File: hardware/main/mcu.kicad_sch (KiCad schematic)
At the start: 0 parts

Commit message: hardware: footprints for every part, LCSC library, real A1S pin plan
- lib/lcsc: ESP32-A1S, NS4150B, FS8205A, MSK12C02, PJ-320D imported
  from LCSC with easyeda2kicad (3D paths fixed, NPTH pegs, A1S antenna
  keepout and courtyard), registered in all three projects.
- Parts table with footprint and LCSC number in hardware/README.md.
- The A1S keeps the codec's I2C/I2S inside: display moves to the
  ST7789's pins 14/13/15/22 (SPI or I2C), LED to 12, CHRG/STDBY to 4/2
  through BAT54W. J_SW and J_CHG for an off-board switch and charge LEDs.
- Block sheets use the module's real outputs (HPOUTL/R, SPOLP/N, SPORP/N).

Co-Authored-By: Claude Opus 5.5 <noreply@anthropic.com>
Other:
- note added: "MCU block. To draw here: ESP32-A1S (ES8388; codec I2C/I2S are inside the module), 22u + 100n, EN 10k + 1u, Boot and Reset buttons, 10k pull-ups on GPIO36/39, 10k pull-down on GPIO12 (LED), display: SCK 14, MOSI/SDA 13, CS 15, DC 22; 4.7k pull-ups on 13/14 fitted for I2C only. CHRG 4, STDBY 2. Unused: MIC/LINEIN pins."
- note removed: "MCU block. To draw here: ESP32-A1S (ES8388), 22u + 100n, EN 10k + 1u, Boot and Reset buttons, status LED (GPIO22), I2C pull-ups 4.7k, 10k pull-ups on GPIO36/39. Unused: GPIO12, 16, 17, 35."
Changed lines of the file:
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@@
 		(rev "A")
 	)
-	(text "MCU block. To draw here:\nESP32-A1S (ES8388), 22u + 100n, EN 10k + 1u, Boot and Reset buttons,\nstatus LED (GPIO22), I2C pull-ups 4.7k, 10k pull-ups on GPIO36/39.\nUnused: GPIO12, 16, 17, 35."
+	(text "MCU block. To draw here:\nESP32-A1S (ES8388; codec I2C/I2S are inside the module), 22u + 100n, EN 10k + 1u,\nBoot and Reset buttons, 10k pull-ups on GPIO36/39, 10k pull-down on GPIO12 (LED),\ndisplay: SCK 14, MOSI/SDA 13, CS 15, DC 22; 4.7k pull-ups on 13/14 fitted for I2C only.\nCHRG 4, STDBY 2. Unused: MIC/LINEIN pins."
 		(exclude_from_sim no)
 		(at 101.6 40.64 0)
@@
 		)
 	)
-	(hierarchical_label "BTN6"
+	(hierarchical_label "U0TXD"
+		(shape output)
+		(at 50.8 55.88 180)
+		(effects
+			(font
+				(size 1.27 1.27)
+			)
+			(justify right)
+		)
+	)
+	(hierarchical_label "LED"
+		(shape output)
+		(at 50.8 172.72 180)
+		(effects
+			(font
+				(size 1.27 1.27)
+			)
+			(justify right)
+		)
+	)
+	(hierarchical_label "BTN1"
 		(shape input)
 		(at 50.8 147.32 180)
@@
 		)
 	)
-	(hierarchical_label "U0TXD"
-		(shape output)
-		(at 50.8 55.88 180)
-		(effects
-			(font
-				(size 1.27 1.27)
-			)
-			(justify right)
-		)
-	)
-	(hierarchical_label "BTN1"
-		(shape input)
-		(at 50.8 127 180)
-		(effects
-			(font
-				(size 1.27 1.27)
-			)
-			(justify right)
-		)
-	)
-	(hierarchical_label "STDBY"
-		(shape input)
-		(at 50.8 76.2 180)
+	(hierarchical_label "CHRG"
+		(shape input)
+		(at 50.8 71.12 180)
 		(effects
 			(font
@@
 	(hierarchical_label "BTN3"
 		(shape input)
-		(at 50.8 132.08 180)
-		(effects
-			(font
-				(size 1.27 1.27)
-			)
-			(justify right)
-		)
-	)
-	(hierarchical_label "SDA"
-		(shape bidirectional)
-		(at 50.8 116.84 180)
-		(effects
-			(font
-				(size 1.27 1.27)
-			)
-			(justify right)
-		)
-	)
-	(hierarchical_label "VBAT_SENSE"
-		(shape input)
-		(at 50.8 81.28 180)
+		(at 50.8 152.4 180)
+		(effects
+			(font
+				(size 1.27 1.27)
+			)
+			(justify right)
+		)
+	)
+	(hierarchical_label "SPORP"
+		(shape output)
+		(at 50.8 106.68 180)
+		(effects
+			(font
+				(size 1.27 1.27)
+			)
+			(justify right)
+		)
+	)
+	(hierarchical_label "DISP_CS"
+		(shape output)
+		(at 50.8 137.16 180)
+		(effects
+			(font
+				(size 1.27 1.27)
+			)
+			(justify right)
+		)
+	)
+	(hierarchical_label "BTN5"
+		(shape input)
+		(at 50.8 162.56 180)
+		(effects
+			(font
+				(size 1.27 1.27)
+			)
+			(justify right)
+		)
+	)
+	(hierarchical_label "HP_DET"
+		(shape input)
+		(at 50.8 121.92 180)
 		(effects
 			(font
@@
 		)
 	)
+	(hierarchical_label "EN"
+		(shape input)
+		(at 50.8 60.96 180)
+		(effects
+			(font
+				(size 1.27 1.27)
+			)
+			(justify right)
+		)
+	)
+	(hierarchical_label "DISP_SCK"
+		(shape output)
+		(at 50.8 127 180)
+		(effects
+			(font
+				(size 1.27 1.27)
+			)
+			(justify right)
+		)
+	)
 	(hierarchical_label "AMP_EN"
 		(shape output)
-		(at 50.8 106.68 180)
+		(at 50.8 116.84 180)
+		(effects
+			(font
+				(size 1.27 1.27)
+			)
+			(justify right)
+		)
+	)
+	(hierarchical_label "SPOLP"
+		(shape output)
+		(at 50.8 96.52 180)
+		(effects
+			(font
+				(size 1.27 1.27)
+			)
+			(justify right)
+		)
+	)
+	(hierarchical_label "VBAT_SENSE"
+		(shape input)
+		(at 50.8 81.28 180)
 		(effects
 			(font
@@
 		)
 	)
-	(hierarchical_label "EN"
-		(shape input)
-		(at 50.8 60.96 180)
-		(effects
-			(font
-				(size 1.27 1.27)
-			)
-			(justify right)
-		)
-	)
-	(hierarchical_label "ROUT1"
+	(hierarchical_label "DISP_MOSI"
+		(shape bidirectional)
+		(at 50.8 132.08 180)
+		(effects
+			(font
+				(size 1.27 1.27)
+			)
+			(justify right)
+		)
+	)
+	(hierarchical_label "HPOUTL"
+		(shape output)
+		(at 50.8 86.36 180)
+		(effects
+			(font
+				(size 1.27 1.27)
+			)
+			(justify right)
+		)
+	)
+	(hierarchical_label "SPOLN"
+		(shape output)
+		(at 50.8 101.6 180)
+		(effects
+			(font
+				(size 1.27 1.27)
+			)
+			(justify right)
+		)
+	)
+	(hierarchical_label "STDBY"
+		(shape input)
+		(at 50.8 76.2 180)
+		(effects
+			(font
+				(size 1.27 1.27)
+			)
+			(justify right)
+		)
+	)
+	(hierarchical_label "BTN4"
+		(shape input)
+		(at 50.8 157.48 180)
+		(effects
+			(font
+				(size 1.27 1.27)
+			)
+			(justify right)
+		)
+	)
+	(hierarchical_label "DISP_DC"
+		(shape output)
+		(at 50.8 142.24 180)
+		(effects
+			(font
+				(size 1.27 1.27)
+			)
+			(justify right)
+		)
+	)
+	(hierarchical_label "HPOUTR"
 		(shape output)
 		(at 50.8 91.44 180)
@@
 		)
 	)
-	(hierarchical_label "LOUT1"
-		(shape output)
-		(at 50.8 86.36 180)
-		(effects
-			(font
-				(size 1.27 1.27)
-			)
-			(justify right)
-		)
-	)
-	(hierarchical_label "BTN5"
-		(shape input)
-		(at 50.8 142.24 180)
-		(effects
-			(font
-				(size 1.27 1.27)
-			)
-			(justify right)
-		)
-	)
-	(hierarchical_label "ROUT2"
-		(shape output)
-		(at 50.8 101.6 180)
-		(effects
-			(font
-				(size 1.27 1.27)
-			)
-			(justify right)
-		)
-	)
-	(hierarchical_label "LOUT2"
-		(shape output)
-		(at 50.8 96.52 180)
-		(effects
-			(font
-				(size 1.27 1.27)
-			)
-			(justify right)
-		)
-	)
-	(hierarchical_label "HP_DET"
-		(shape input)
+	(hierarchical_label "SPORN"
+		(shape output)
 		(at 50.8 111.76 180)
 		(effects
@@
 		)
 	)
-	(hierarchical_label "CHRG"
-		(shape input)
-		(at 50.8 71.12 180)
-		(effects
-			(font
-				(size 1.27 1.27)
-			)
-			(justify right)
-		)
-	)
-	(hierarchical_label "LED"
-		(shape output)
-		(at 50.8 152.4 180)
-		(effects
-			(font
-				(size 1.27 1.27)
-			)
-			(justify right)
-		)
-	)
-	(hierarchical_label "SCL"
-		(shape output)
-		(at 50.8 121.92 180)
-		(effects
-			(font
-				(size 1.27 1.27)
-			)
-			(justify right)
-		)
-	)
-	(hierarchical_label "BTN4"
-		(shape input)
-		(at 50.8 137.16 180)
-		(effects
-			(font
+	(hierarchical_label "BTN6"
+		(shape input)
+		(at 50.8 167.64 180)
+		(effects
+			(font

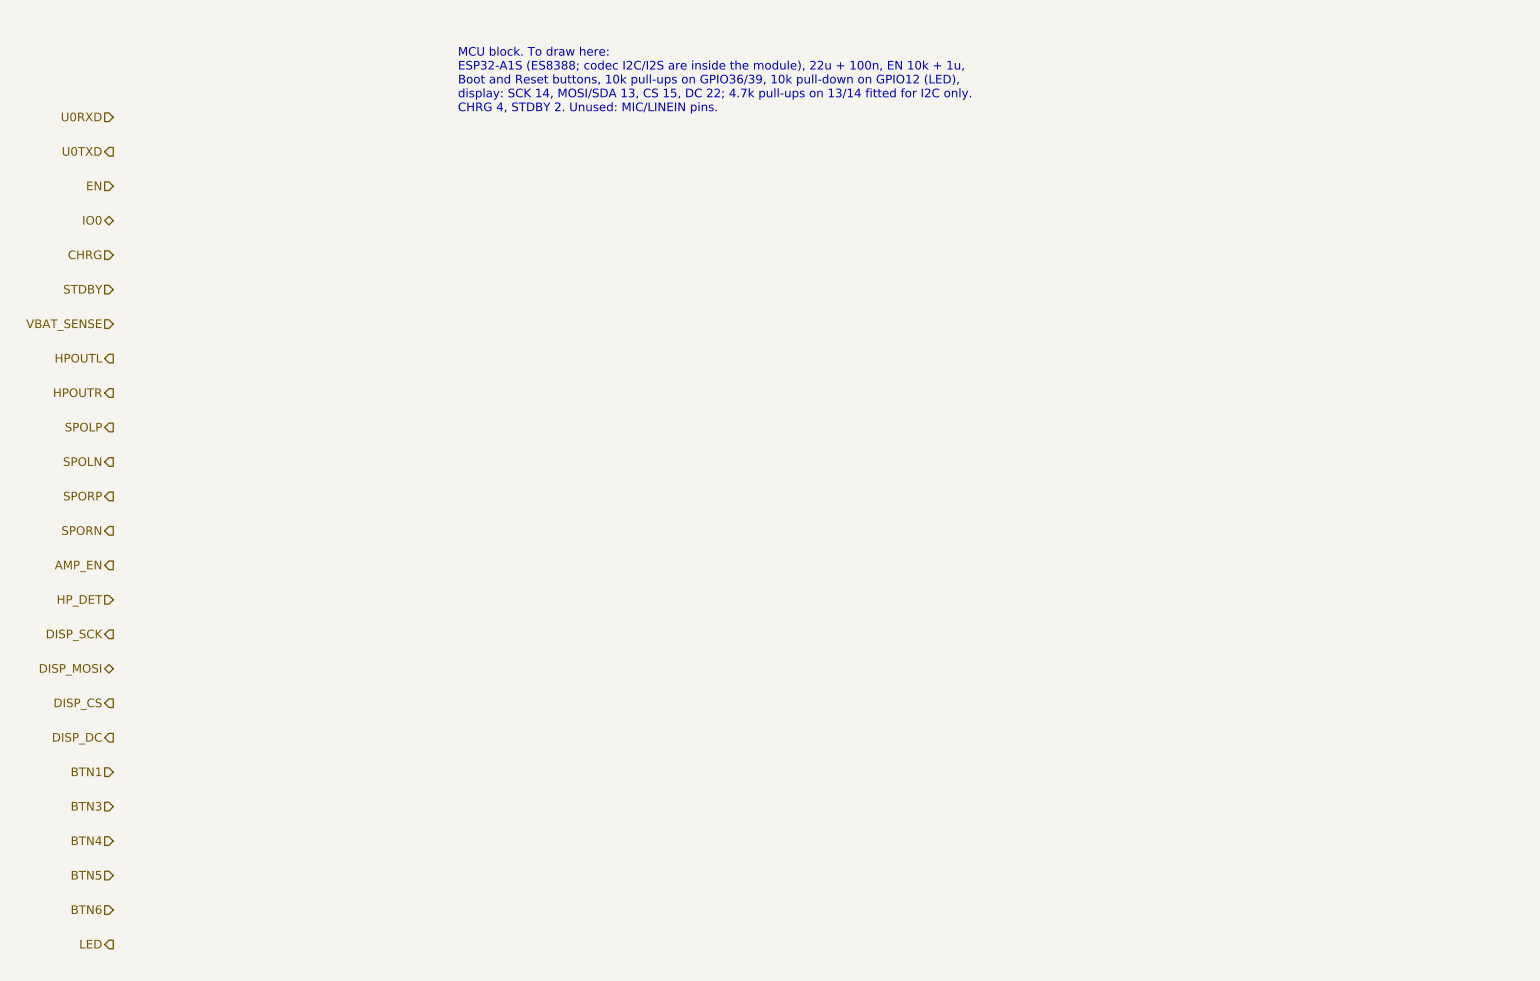
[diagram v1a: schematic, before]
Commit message: hardware: MCU sheet (ESP32-A1S, EN/Boot/Reset, pull-ups, status LED)
Co-Authored-By: Claude Opus 5.5 <noreply@anthropic.com>
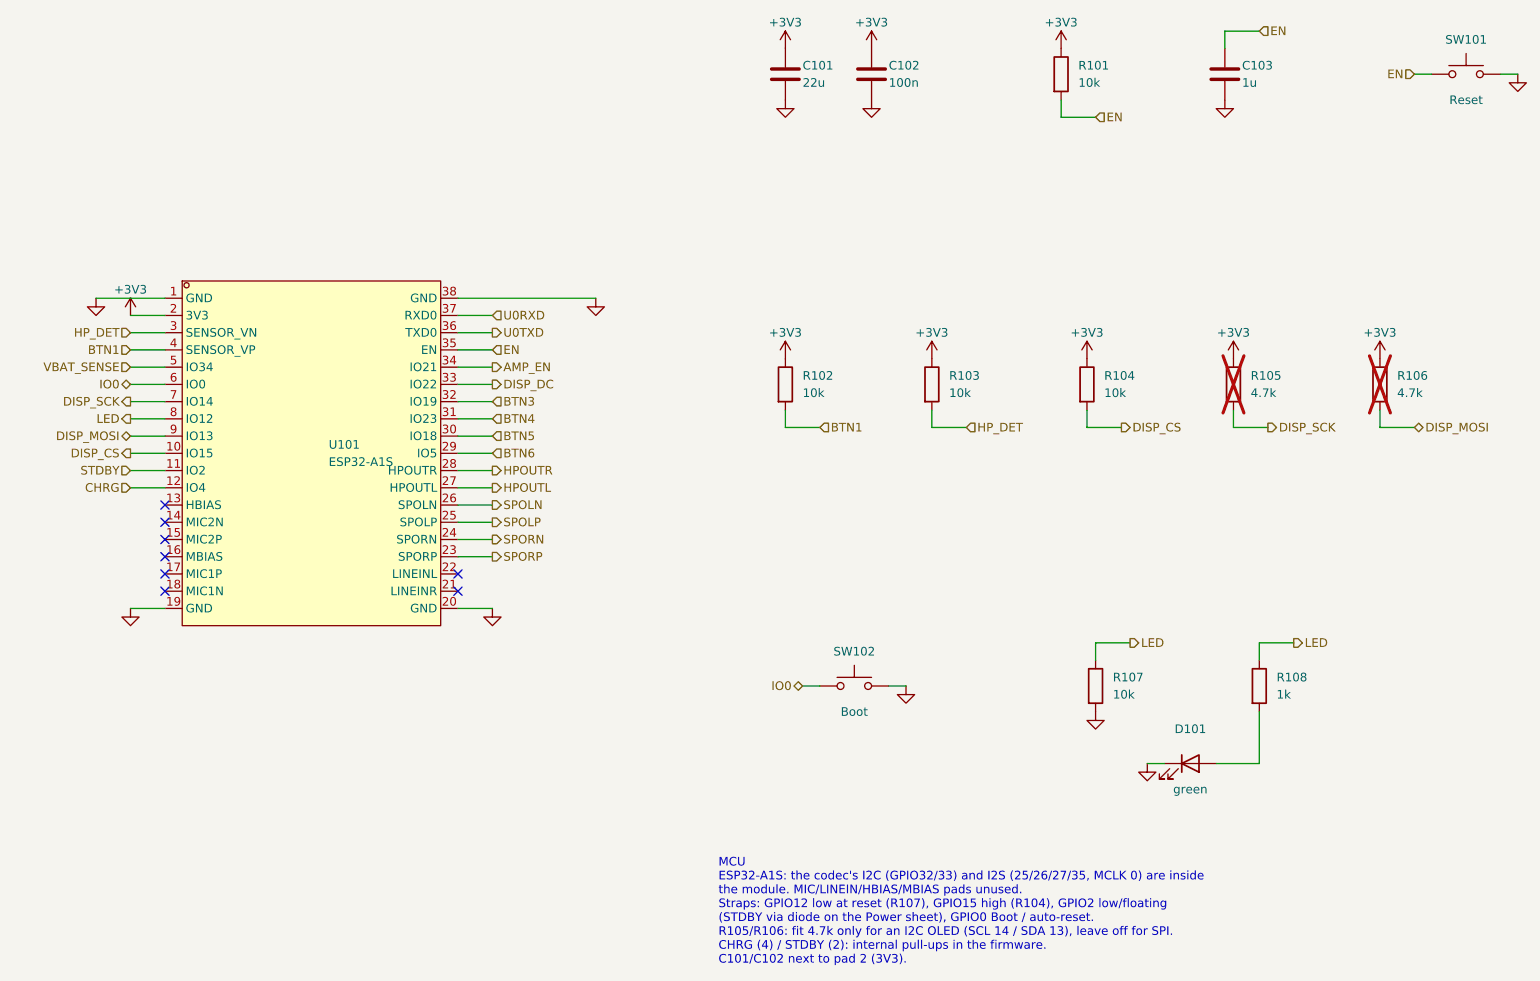
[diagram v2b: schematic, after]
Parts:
- added C101: 22u, Capacitor_SMD:C_0805_2012Metric, symbol Device:C
- added C102: 100n, Capacitor_SMD:C_0805_2012Metric, symbol Device:C
- added C103: 1u, Capacitor_SMD:C_0805_2012Metric, symbol Device:C
- added D101: green, LED_SMD:LED_0805_2012Metric, symbol Device:LED
- added R101, R102, R103, R104, R107: 10k, Resistor_SMD:R_0805_2012Metric, symbol Device:R
- added R105, R106: 4.7k, Resistor_SMD:R_0805_2012Metric, symbol Device:R
- added R108: 1k, Resistor_SMD:R_0805_2012Metric, symbol Device:R
- added SW101: Reset, Button_Switch_SMD:SW_Push_1P1T_XKB_TS-1187A, symbol Switch:SW_Push
- added SW102: Boot, Button_Switch_SMD:SW_Push_1P1T_XKB_TS-1187A, symbol Switch:SW_Push
- added U101: ESP32-A1S, lcsc:WIRELM-SMD_ESP32-A1S, symbol lcsc:ESP32-A1S
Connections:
- net AMP_EN: now also U101.34 (IO21)
- net BTN1: now also R102.2, U101.4 (SENSOR_VP)
- net BTN3: now also U101.32 (IO19)
- net BTN4: now also U101.31 (IO23)
- net BTN5: now also U101.30 (IO18)
- net BTN6: now also U101.29 (IO5)
- net CHRG: now also U101.12 (IO4)
- net DISP_CS: now also R104.2, U101.10 (IO15)
- net DISP_DC: now also U101.33 (IO22)
- net DISP_MOSI: now also R106.2, U101.9 (IO13)
- net DISP_SCK: now also R105.2, U101.7 (IO14)
- net EN: now also C103.1, R101.2, SW101.1, U101.35 (EN)
- net HPOUTL: now also U101.27 (HPOUTL)
- net HPOUTR: now also U101.28 (HPOUTR)
- net HP_DET: now also R103.2, U101.3 (SENSOR_VN)
- net IO0: now also SW102.1, U101.6 (IO0)
- net LED: now also R107.1, R108.1, U101.8 (IO12)
- net SPOLN: now also U101.26 (SPOLN)
- net SPOLP: now also U101.25 (SPOLP)
- net SPORN: now also U101.24 (SPORN)
- net SPORP: now also U101.23 (SPORP)
- net STDBY: now also U101.11 (IO2)
- net U0RXD: now also U101.37 (RXD0)
- net U0TXD: now also U101.36 (TXD0)
- net VBAT_SENSE: now also U101.5 (IO34)
- new net: D101.2 (A), R108.2
- new net +3V3: C101.1, C102.1, R101.1, R102.1, R103.1, R104.1, R105.1, R106.1, U101.2 (3V3)
- new net GND: C101.2, C102.2, C103.2, D101.1 (K), R107.2, SW101.2, SW102.2, U101.1 (GND), U101.19 (GND), U101.20 (GND), U101.38 (GND)
- no-connect marks 0 -> 8
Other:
- note added: "MCU ESP32-A1S: the codec's I2C (GPIO32/33) and I2S (25/26/27/35, MCLK 0) are inside the module. MIC/LINEIN/HBIAS/MBIAS pads unused. Straps: GPIO12 low at reset (R107), GPIO15 high (R104), GPIO2 low/floating (STDBY via diode on the Power sheet), GPIO0 Boot / auto-reset. R105/R106: fit 4.7k only for an I2C OLED (SCL 14 / SDA 13), leave off for SPI. CHRG (4) / STDBY (2): internal pull-ups in the fir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"
- note removed: "MCU block. To draw here: ESP32-A1S (ES8388; codec I2C/I2S are inside the module), 22u + 100n, EN 10k + 1u, Boot and Reset buttons, 10k pull-ups on GPIO36/39, 10k pull-down on GPIO12 (LED), display: SCK 14, MOSI/SDA 13, CS 15, DC 22; 4.7k pull-ups on 13/14 fitted for I2C only. CHRG 4, STDBY 2. Unused: MIC/LINEIN pins."

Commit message: hardware: main board routed and labelled, JLC files
- Freerouting (jar, portable Java 25) via scripts/route.py; net classes
  Power 0.8 mm / Supply 0.4 mm so tracks fit the fine-pitch pins.
- Silkscreen pin names and function labels (silk_main.py), references on
  the fab layer, SMD GND pads solid to the pour; board 100 x 58 mm.
- LCSC numbers on all SMD parts (checked on lcsc.com); jlc.py writes the
  Gerber ZIP, BOM and CPL in JLC's formats.

Co-Authored-By: Claude Opus 5.5 <noreply@anthropic.com>
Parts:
- C101: LCSC (none) -> C45783
- C102: LCSC (none) -> C49678
- C103: LCSC (none) -> C28323
- D101: LCSC (none) -> C2297
- R101, R102, R103, R104, R107: LCSC (none) -> C17414
- R105, R106: LCSC (none) -> C17673
- R108: LCSC (none) -> C17513
- SW101, SW102: LCSC (none) -> C318884
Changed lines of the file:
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@@
+			)
+		)
+		(property "LCSC" "C17414"
+			(at 0 0 0)
+			(hide yes)
+			(effects
+				(font
+					(size 1.27 1.27)
+				)
 			)
 		)
@@
 			)
 		)
+		(property "LCSC" "C28323"
+			(at 0 0 0)
+			(hide yes)
+			(effects
+				(font
+					(size 1.27 1.27)
+				)
+			)
+		)
 		(property "Description" ""
 			(at 214.63 44.45 0)
@@
 			(show_name no)
 			(do_not_autoplace no)
+			(effects
+				(font
+					(size 1.27 1.27)
+				)
+			)
+		)
+		(property "LCSC" "C17414"
+			(at 0 0 0)
+			(hide yes)
 			(effects
 				(font
@@
 			)
 		)
+		(property "LCSC" "C17673"
+			(at 0 0 0)
+			(hide yes)
+			(effects
+				(font
+					(size 1.27 1.27)
+				)
+			)
+		)
 		(property "Description" ""
 			(at 237.49 90.17 0)
@@
 			)
 		)
+		(property "LCSC" "C2297"
+			(at 0 0 0)
+			(hide yes)
+			(effects
+				(font
+					(size 1.27 1.27)
+				)
+			)
+		)
 		(property "Description" ""
 			(at 209.55 146.05 0)
@@
 			)
 		)
+		(property "LCSC" "C318884"
+			(at 0 0 0)
+			(hide yes)
+			(effects
+				(font
+					(size 1.27 1.27)
+				)
+			)
+		)
 		(property "Description" ""
 			(at 160.02 134.62 0)
@@
 			)
 		)
+		(property "LCSC" "C17513"
+			(at 0 0 0)
+			(hide yes)
+			(effects
+				(font
+					(size 1.27 1.27)
+				)
+			)
+		)
 		(property "Description" ""
 			(at 219.71 134.62 0)
@@
 			)
 		)
+		(property "LCSC" "C49678"
+			(at 0 0 0)
+			(hide yes)
+			(effects
+				(font
+					(size 1.27 1.27)
+				)
+			)
+		)
 		(property "Description" ""
 			(at 162.56 44.45 0)
@@
 			)
 		)
+		(property "LCSC" "C318884"
+			(at 0 0 0)
+			(hide yes)
+			(effects
+				(font
+					(size 1.27 1.27)
+				)
+			)
+		)
 		(property "Description" ""
 			(at 250.19 44.45 0)
@@
 			(show_name no)
 			(do_not_autoplace no)
+			(effects
+				(font
+					(size 1.27 1.27)
+				)
+			)
+		)
+		(property "LCSC" "C17414"
+			(at 0 0 0)
+			(hide yes)
 			(effects
 				(font
@@
 			)
 		)
+		(property "LCSC" "C17673"
+			(at 0 0 0)
+			(hide yes)
+			(effects
+				(font
+					(size 1.27 1.27)
+				)
+			)
+		)
 		(property "Description" ""
 			(at 215.9 90.17 0)
@@
 			)
 		)
+		(property "LCSC" "C17414"
+			(at 0 0 0)
+			(hide yes)
+			(effects
+				(font
+					(size 1.27 1.27)
+				)
+			)
+		)
 		(property "Description" ""
 			(at 171.45 90.17 0)
@@
 			)
 		)
+		(property "LCSC" "C17414"
+			(at 0 0 0)
+			(hide yes)
+			(effects
+				(font
+					(size 1.27 1.27)
+				)
+			)
+		)
 		(property "Description" ""
 			(at 195.58 134.62 0)
@@
 			(effects
 				(font
+					(size 1.27 1.27)
+				)
+			)
+		)
+		(property "LCSC" "C45783"
+			(at 0 0 0)
+			(hide yes)
+			(effects
+				(font
